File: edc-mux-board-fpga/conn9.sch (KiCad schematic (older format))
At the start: 24 parts

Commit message: Finished FPGA and MCU interconnections.
Finished up interrupt wiring
Fixed a few missing connections
Annotated Schematic
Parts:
- removed C? (x2): 1uF, Capacitor_SMD:C_0805_2012Metric, symbol Device:C_Small
- removed C? (x2): 2.2uF X7R, Capacitor_SMD:C_0603_1608Metric, symbol Device:C_Small
- removed C? (x2): 1uF, Capacitor_SMD:C_0603_1608Metric, symbol Device:C_Small
- removed C? (x8): 100nF, Capacitor_SMD:C_0603_1608Metric, symbol Device:C_Small
- removed C? (x2): 33pF, Capacitor_SMD:C_0603_1608Metric, symbol Device:C_Small
- removed C? (x2): 10uF, Capacitor_SMD:C_1206_3216Metric, symbol Device:C_Small
- removed FB?: 220Ω/2A, Resistor_SMD:R_0603_1608Metric, symbol Device:Ferrite_Bead_Small
- removed R? (x2): 750Ω, Resistor_SMD:R_0603_1608Metric, symbol Device:R_Small_US
- removed U?: TLV320AIC3206, Package_DFN_QFN:UQFN-40-1EP_5x5mm_P0.4mm_EP3.8x3.8mm_ThermalVias, symbol SW-Texas:TLV320AIC3206
- removed U?: MAX4910, Package_DFN_QFN:TQFN-16-1EP_3x3mm_P0.5mm_EP1.23x1.23mm, symbol SW-dallas-semi-maxim:MAX4910
- removed U?: P82B96, Package_SO:TSSOP-8_3x3mm_P0.65mm, symbol Interface_Expansion:P82B96
- added C167, C184: 2.2uF X7R, Capacitor_SMD:C_0603_1608Metric, symbol Device:C_Small
- added C168, C170, C171, C174, C175, C176, C177, C182: 100nF, Capacitor_SMD:C_0603_1608Metric, symbol Device:C_Small
- added C169, C179: 10uF, Capacitor_SMD:C_1206_3216Metric, symbol Device:C_Small
- added C172, C173: 33pF, Capacitor_SMD:C_0603_1608Metric, symbol Device:C_Small
- added C178, C183: 1uF, Capacitor_SMD:C_0603_1608Metric, symbol Device:C_Small
- added C180, C181: 1uF, Capacitor_SMD:C_0805_2012Metric, symbol Device:C_Small
- added FB12: 220Ω/2A, Resistor_SMD:R_0603_1608Metric, symbol Device:Ferrite_Bead_Small
- added R33, R34: 750Ω, Resistor_SMD:R_0603_1608Metric, symbol Device:R_Small_US
- added U31: MAX4910, Package_DFN_QFN:TQFN-16-1EP_3x3mm_P0.5mm_EP1.23x1.23mm, symbol SW-dallas-semi-maxim:MAX4910
- added U32: TLV320AIC3206, Package_DFN_QFN:UQFN-40-1EP_5x5mm_P0.4mm_EP3.8x3.8mm_ThermalVias, symbol SW-Texas:TLV320AIC3206
- added U33: P82B96, Package_SO:TSSOP-8_3x3mm_P0.65mm, symbol Interface_Expansion:P82B96
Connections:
- net +12V: now also C182.1, R33.1, R34.1, U33.8 (VCC)
- net +1V8: now also C170.2, C174.2, U32.30 (VSYS), U32.40 (DVDD)
- net +1V8A: now also C177.2, C178.2, C179.2, U32.29 (AVDD), U32.32 (DRVDD_HP), U32.39 (DVDD_CP)
- net +3V3: now also C168.2, C169.1, C171.2, U31.14 (VCC), U32.10 (IOVDD)
- net AUD_GND: now also U31.4 (COM2)
- net BCLK: now also U32.6 (BCLK)
- net DIN: now also U32.8 (DIN)
- net DOUT: now also U32.9 (DOUT)
- net GND: now also C168.1, C169.2, C170.1, C171.1, C172.1, C173.1, C174.1, C175.1, C176.1, C177.1, C178.1, C179.1, C182.2, C183.1, C184.1, FB12.2, U31.17 (PAD), U31.5 (NC2), U31.6 (GND), U32.1 (DVSS), U32.11 (IOVSS), U32.16 (SPI_SELECT), U32.2 (DVSS), U32.21 (AVSS), U32.37 (DVSS_CP), U32.41 (PAD), U33.4 (GND)
- net HP_~LINE~_SEL: now also U31.10 (CB2), U31.2 (CB1), U32.4 (INT2_OUT)
- net L_IN: now also C172.2, U32.17 (IN1_L)
- net L_OUT: now also U31.16 (COM1)
- net MCLK: now also U32.5 (MCLK)
- net R_IN: now also C173.2, U32.18 (IN1_R)
- net R_OUT: now also U31.8 (COM3)
- net SCL: now also U32.13 (SCL), U33.7 (SCL)
- net SCL_HV: now also R34.2, U33.5 (TXD-SCL), U33.6 (RXD-SCL)
- net SDA: now also U32.14 (SDA), U33.1 (SDA)
- net SDA_HV: now also R33.2, U33.2 (RXD-SDA), U33.3 (TXD-SDA)
- net WCLK: now also U32.7 (WCLK)
- net ~RESET: now also U32.3 (~RESET)
- new net: C180.1, U31.1 (NC1)
- new net: C180.2, U32.26 (LINE_OUT_L)
- new net: C181.1, U31.9 (NC3)
- new net: C181.2, U32.27 (LINE_OUT_R)
- new net: C175.2, U32.19 (IN2_L), U32.20 (IN2_R)
- new net: C183.2, U32.22 (REF)
- new net: C176.2, U32.24 (IN3_L), U32.25 (IN3_R)
- new net: FB12.1, U31.3 (NO2), U32.28 (GND_SENSE)
- new net: U31.15 (NO1), U32.31 (HPL)
- new net: U31.7 (NO3), U32.33 (HPR)
- new net: C184.2, U32.35 (VNEG)
- new net: C167.1, U32.36 (FLY_N)
- new net: C167.2, U32.38 (FLY_P)

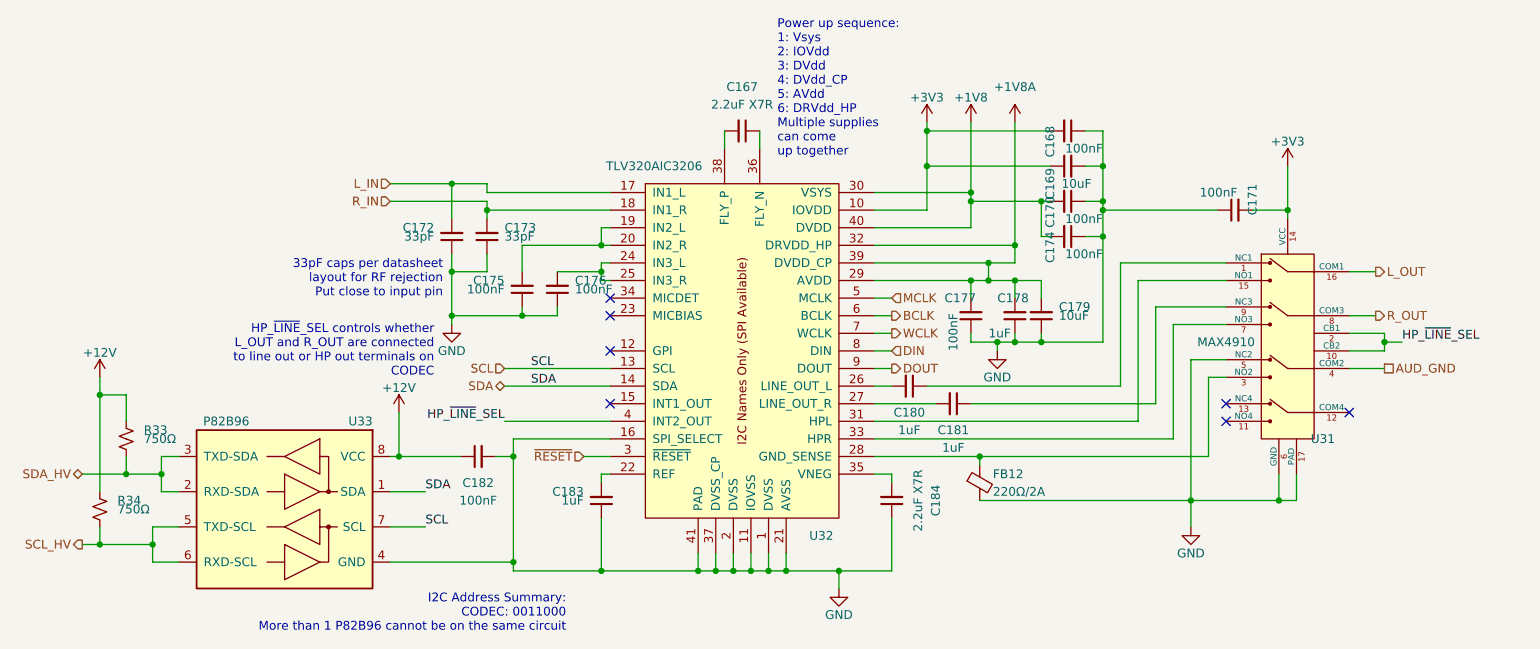
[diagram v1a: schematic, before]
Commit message: assigned more footprints
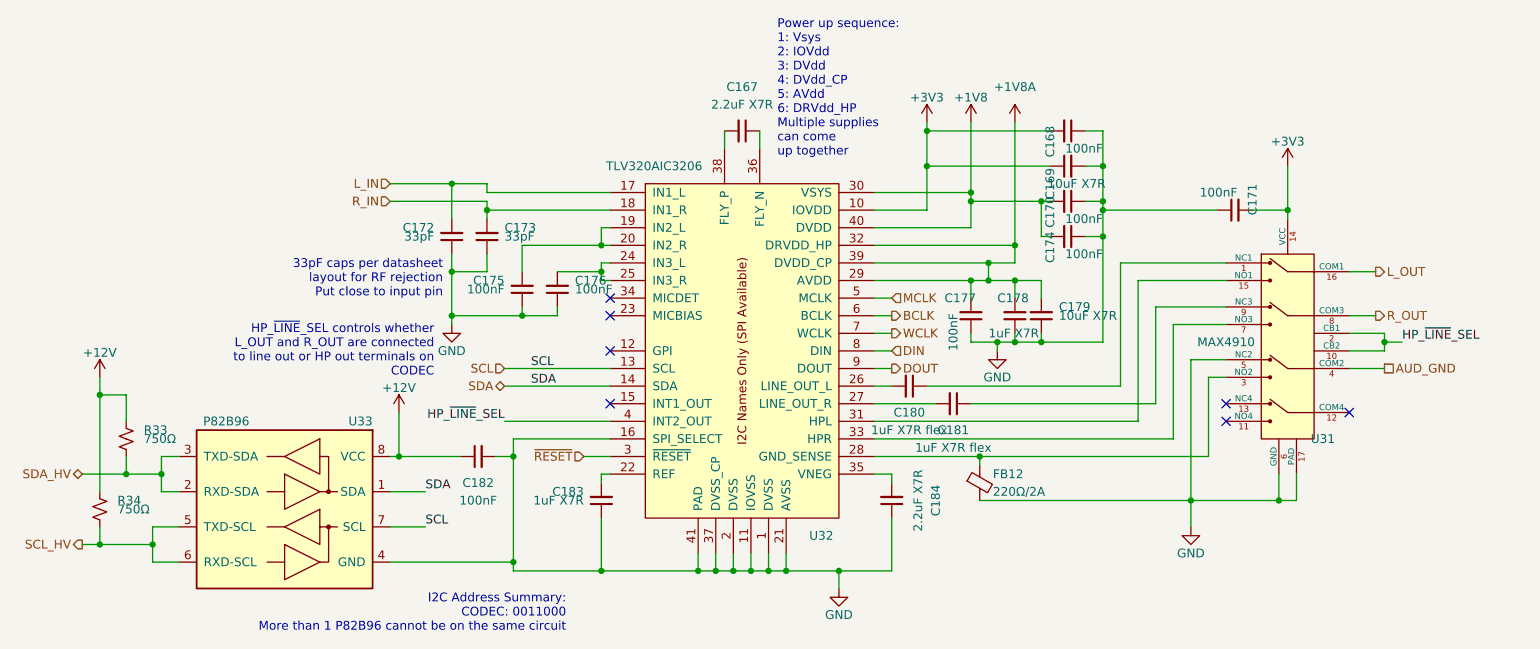
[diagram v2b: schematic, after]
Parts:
- C169, C179: value 10uF -> 10uF X7R
- C178, C183: value 1uF -> 1uF X7R
- C180, C181: value 1uF -> 1uF X7R flex
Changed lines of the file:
@@
 P 4400 4250
 F 0 "C183" H 4500 4200 50  0000 L CNN
-F 1 "1uF" H 4500 4250 50  0000 L CNN
+F 1 "1uF X7R" H 4500 4250 50  0000 L CNN
 F 2 "Capacitor_SMD:C_0603_1608Metric" H 4400 4250 50  0001 C CNN
 F 3 "~" H 4400 4250 50  0001 C CNN
@@
 P 6750 3200
 F 0 "C178" H 6850 3100 50  0000 R CNN
-F 1 "1uF" H 6900 3300 50  0000 R CNN
+F 1 "1uF X7R" H 6900 3300 50  0000 R CNN
 F 2 "Capacitor_SMD:C_0603_1608Metric" H 6750 3200 50  0001 C CNN
 F 3 "~" H 6750 3200 50  0001 C CNN
@@
 P 6900 3200
 F 0 "C179" H 6800 3150 50  0000 R CNN
-F 1 "10uF" H 6800 3200 50  0000 R CNN
+F 1 "10uF X7R" H 6800 3200 50  0000 R CNN
 F 2 "Capacitor_SMD:C_1206_3216Metric" H 6900 3200 50  0001 C CNN
 F 3 "~" H 6900 3200 50  0001 C CNN
@@
 P 7050 2350
 F 0 "C169" H 6950 2450 50  0000 C CNN
-F 1 "10uF" V 6950 2300 50  0000 C CNN
+F 1 "10uF X7R" V 6950 2300 50  0000 C CNN
 F 2 "Capacitor_SMD:C_1206_3216Metric" H 7050 2350 50  0001 C CNN
 F 3 "~" H 7050 2350 50  0001 C CNN
@@
 P 6150 3600
 F 0 "C180" V 6300 3600 50  0000 C CNN
-F 1 "1uF" V 6400 3600 50  0000 C CNN
+F 1 "1uF X7R flex" V 6400 3600 50  0000 C CNN
 F 2 "Capacitor_SMD:C_0805_2012Metric" H 6150 3600 50  0001 C CNN
 F 3 "~" H 6150 3600 50  0001 C CNN
@@
 P 6400 3700
 F 0 "C181" V 6550 3700 50  0000 C CNN
-F 1 "1uF" V 6650 3700 50  0000 C CNN
+F 1 "1uF X7R flex" V 6650 3700 50  0000 C CNN
 F 2 "Capacitor_SMD:C_0805_2012Metric" H 6400 3700 50  0001 C CNN
 F 3 "~" H 6400 3700 50  0001 C CNN

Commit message: re-annotating after adding power ICs and decoupling capacitors.
Also verified most footprints, and updated schematic field data.
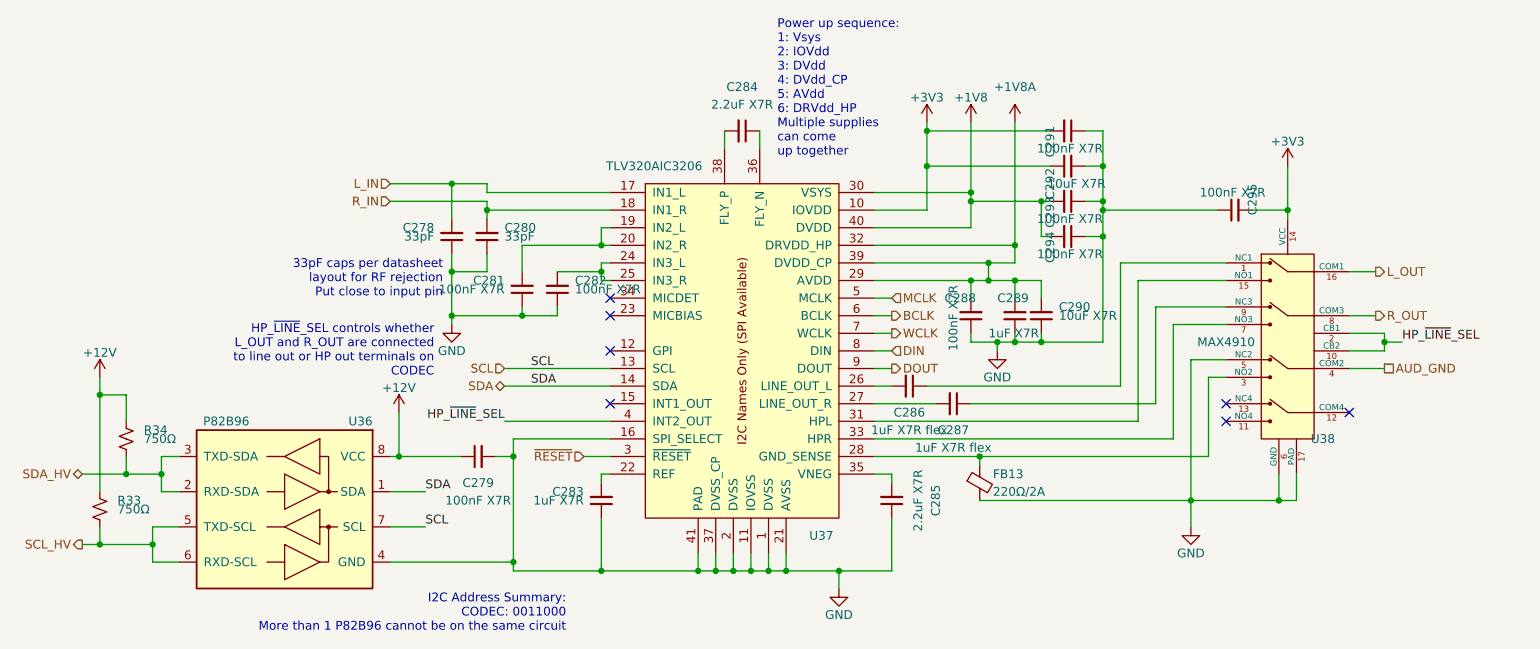
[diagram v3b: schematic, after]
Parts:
- C279: renamed from C182; value 100nF -> 100nF X7R
- C281: renamed from C175; value 100nF -> 100nF X7R
- C282: renamed from C176; value 100nF -> 100nF X7R
- C288: renamed from C177; value 100nF -> 100nF X7R
- C291: renamed from C168; value 100nF -> 100nF X7R
- C293: renamed from C170; value 100nF -> 100nF X7R
- C294: renamed from C174; value 100nF -> 100nF X7R
- C295: renamed from C171; value 100nF -> 100nF X7R
- R33: renamed from R34; Package ID (none) -> 0402in/1005mm
- R34: renamed from R33; Package ID (none) -> 0402in/1005mm
- renumbered C172 to C278, C173 to C280, C183 to C283, C167 to C284, C184 to C285, C180 to C286, C181 to C287, C178 to C289, C179 to C290, C169 to C292, FB12 to FB13, U33 to U36, U32 to U37, U31 to U38

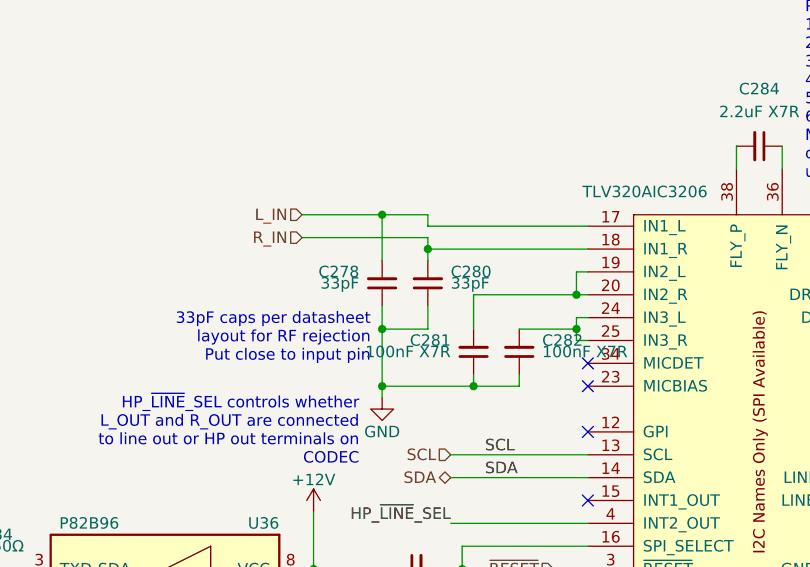
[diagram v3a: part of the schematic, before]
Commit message: Reannotating and adding more fields to components
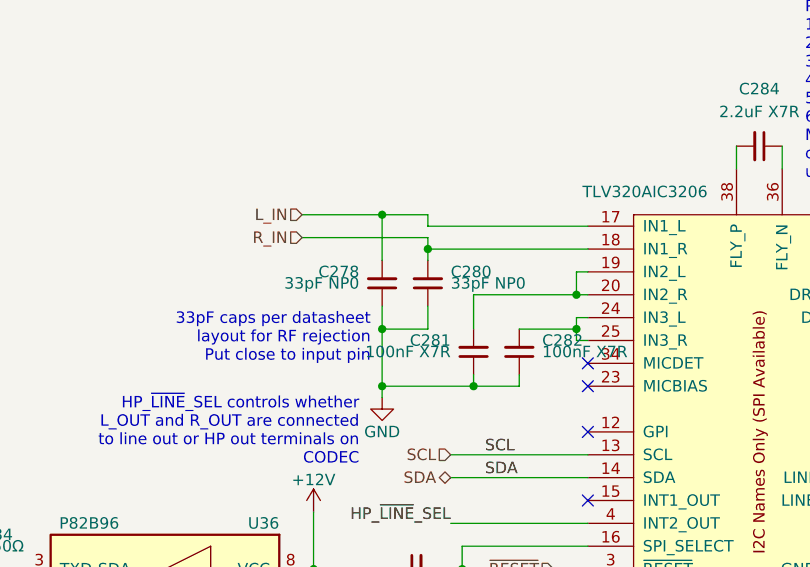
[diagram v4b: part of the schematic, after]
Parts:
- C278, C280: value 33pF -> 33pF NP0; footprint Capacitor_SMD:C_0603_1608Metric -> Capacitor_SMD:C_0402_1005Metric; Characteristics (none) -> CAP CER 33PF 25V NP0 0402; Description (none) -> MLCC Capacitor; Manufacturer (none) -> AVX; Manufacturers Part Number (none) -> 04023A330FAT2A; Package ID 0603in/1608mm -> 0402in/1005mm
- C279, C281, C282, C288, C291, C293, C294, C295: Characteristics (none) -> CAP CER 0.1UF 25V X7R 0603; Description (none) -> MLCC Capacitor; Manufacturer (none) -> Kemet; Manufacturers Part Number (none) -> C0603C104J3RACAUTO
- C283, C289: Characteristics (none) -> CAP CER 1UF 25V X7R 0603; Description (none) -> MLCC Capacitor
- C284, C285: footprint Capacitor_SMD:C_0603_1608Metric -> Capacitor_SMD:C_0805_2012Metric; Characteristics (none) -> CAP CER 2.2UF 25V X7R 0805; Description (none) -> MLCC Capacitor; Manufacturer (none) -> TDK; Manufacturers Part Number (none) -> CGA4J3X7R1E225K125AB; Package ID 0603in/1608mm -> 0805in/2012mm
- C286, C287: Characteristics (none) -> CAP CER 0805 1UF 25V X7R 5%; Description (none) -> MLCC Capacitor; Manufacturers Part Number C0805X105J3RACAUTO -> C0805X105J3RECAUTO
- C290, C292: Characteristics (none) -> CAP CER 10UF 25V X7R 1206; Description (none) -> MLCC Capacitor
- FB13: footprint Resistor_SMD:R_0603_1608Metric -> Inductor_SMD:L_0603_1608Metric; Description (none) -> Ferrite Bead
- R33, R34: Description (none) -> Resistor
- U36: Description (none) -> I2C Buffer / Voltage Translator; Manufacturer (none) -> Texas Instruments; Manufacturers Part Number (none) -> P82B96; Package ID (none) -> TSSOP8
- U37: Description (none) -> I2S Audio Codec; Manufacturer (none) -> Texas Instruments; Package ID (none) -> UQFN40
- U38: Description (none) -> Clickless Audio Switch; Manufacturer (none) -> Maxim Integrated; Package ID (none) -> TQFN16

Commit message: Fixed resistor footprint
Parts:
- R33, R34: footprint Resistor_SMD:R_0603_1608Metric -> Resistor_SMD:R_0402_1005Metric
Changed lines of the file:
@@
 F 0 "R34" H 1800 3950 50  0000 L CNN
 F 1 "750Ω" H 1800 3900 50  0000 L CNN
-F 2 "Resistor_SMD:R_0603_1608Metric" H 1700 3900 50  0001 C CNN
+F 2 "Resistor_SMD:R_0402_1005Metric" H 1700 3900 50  0001 C CNN
 F 3 "~" H 1700 3900 50  0001 C CNN
 F 4 "0402in/1005mm" H 0   0   50  0001 C CNN "Package ID"
@@
 F 0 "R33" H 1650 4350 50  0000 L CNN
 F 1 "750Ω" H 1650 4300 50  0000 L CNN
-F 2 "Resistor_SMD:R_0603_1608Metric" H 1550 4300 50  0001 C CNN
+F 2 "Resistor_SMD:R_0402_1005Metric" H 1550 4300 50  0001 C CNN
 F 3 "~" H 1550 4300 50  0001 C CNN
 F 4 "0402in/1005mm" H 0   0   50  0001 C CNN "Package ID"
